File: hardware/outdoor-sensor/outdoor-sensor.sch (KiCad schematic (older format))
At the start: 11 parts, among them J1 POWER, J2 UART, SW1 RESET, SW2 BOOT, U1 ESP32-WROOM-32, U2 DS18B20

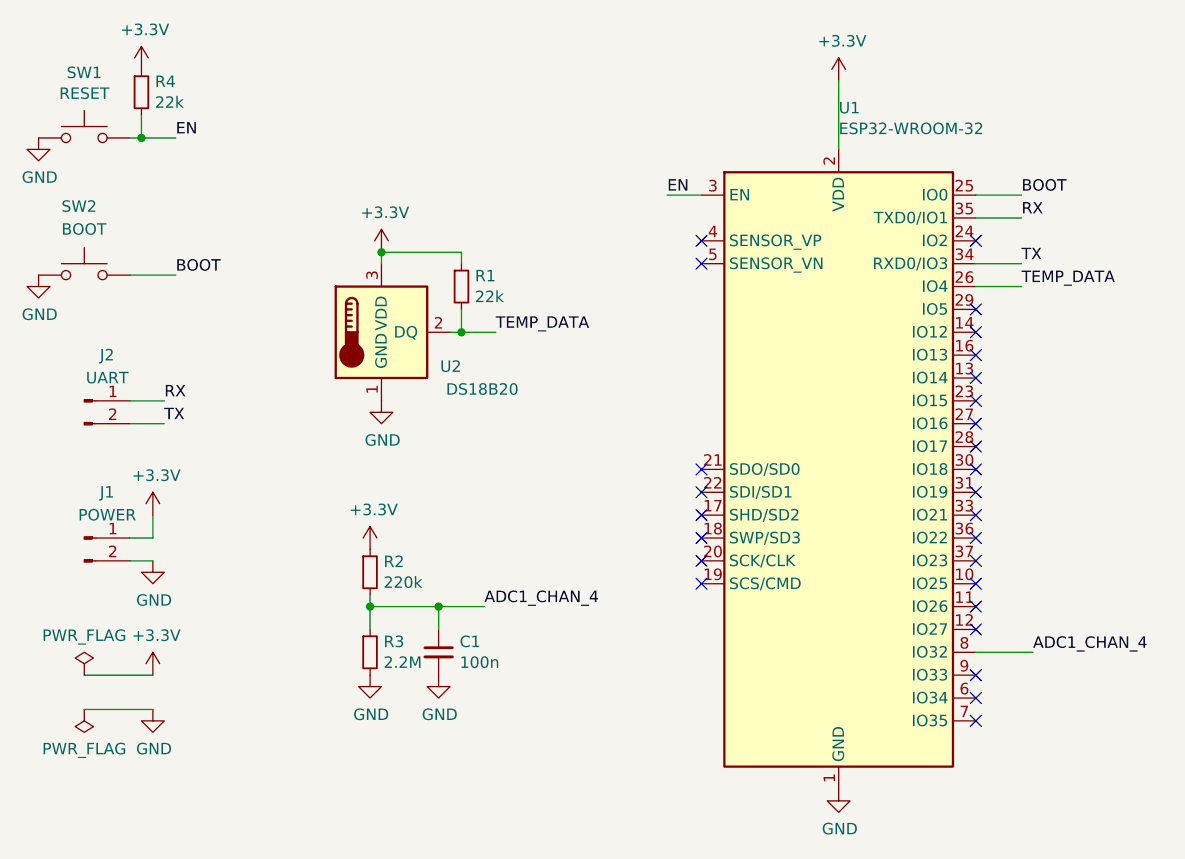
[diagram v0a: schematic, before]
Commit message: Swap out DS18B20 for DS18B20-PAR
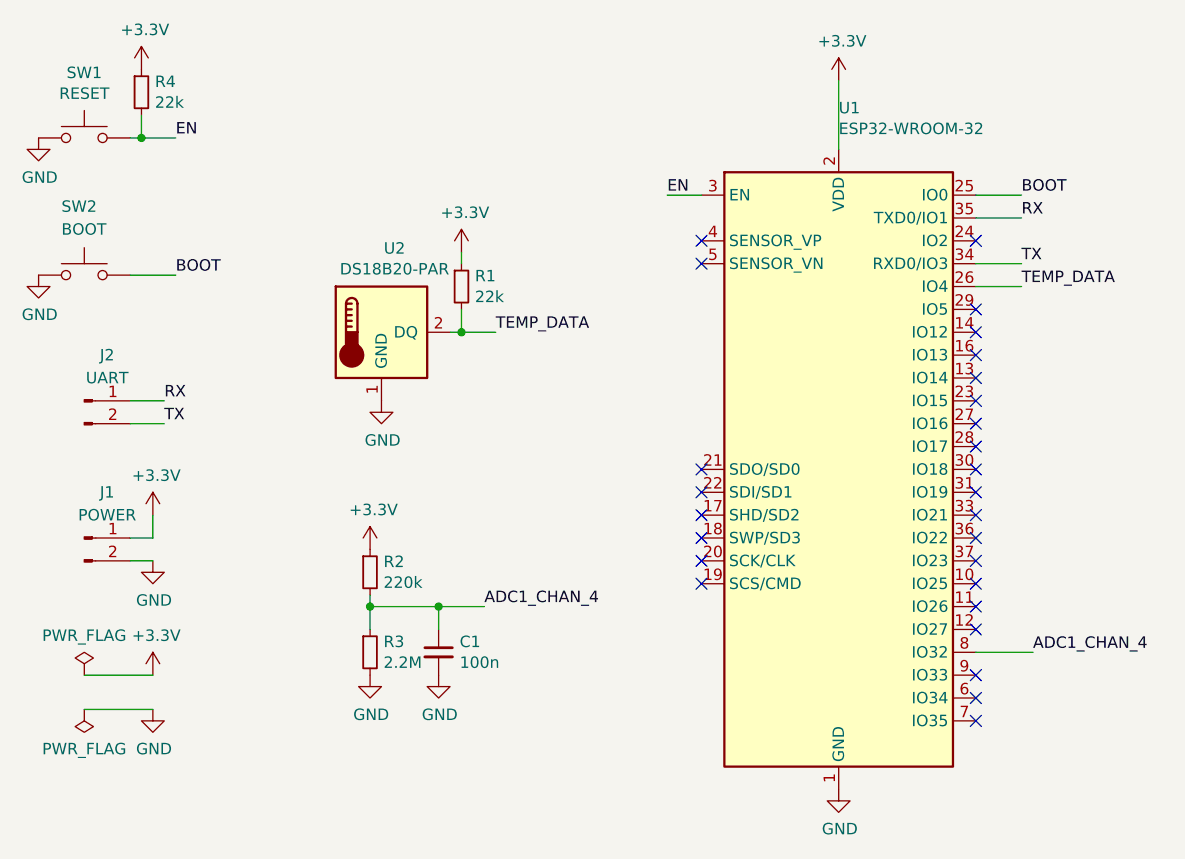
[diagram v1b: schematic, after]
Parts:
- removed U2: DS18B20, Package_TO_SOT_THT:TO-92_Inline, symbol Sensor_Temperature:DS18B20
- added U2: DS18B20-PAR, Package_TO_SOT_THT:TO-92_Inline, symbol Sensor_Temperature:DS18B20-PAR
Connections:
- net GND: now also U2.1 (GND)
- net TEMP_DATA: now also U2.2 (DQ)
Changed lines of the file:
@@
-	1    0    0    -1
-$EndComp
-$Comp
-L Sensor_Temperature:DS18B20 U2
-U 1 1 61550BDD
-P 4250 3050
-F 0 "U2" H 4600 2900 50  0000 R CNN
-F 1 "DS18B20" H 4850 2800 50  0000 R CNN
-F 2 "Package_TO_SOT_THT:TO-92_Inline" H 3250 2800 50  0001 C CNN
-F 3 "http://datasheets.maximintegrated.com/en/ds/DS18B20.pdf" H 4100 3300 50  0001 C CNN
-	1    4250 3050
 	1    0    0    -1
 $EndComp
@@
 L power:+3.3V #PWR0108
 U 1 1 61552A13
-P 4250 2700
-F 0 "#PWR0108" H 4250 2550 50  0001 C CNN
-F 1 "+3.3V" H 4265 2873 50  0000 C CNN
-F 2 "" H 4250 2700 50  0001 C CNN
-F 3 "" H 4250 2700 50  0001 C CNN
-	1    4250 2700
+P 4600 2700
+F 0 "#PWR0108" H 4600 2550 50  0001 C CNN
+F 1 "+3.3V" H 4615 2873 50  0000 C CNN
+F 2 "" H 4600 2700 50  0001 C CNN
+F 3 "" H 4600 2700 50  0001 C CNN
+	1    4600 2700
 	1    0    0    -1
 $EndComp
@@
 	4600 2950 4600 3050
 Wire Wire Line
-	4250 2700 4600 2700
-Wire Wire Line
 	4600 2700 4600 2750
-Wire Wire Line
-	4250 2700 4250 2750
-Connection ~ 4250 2700
 Wire Wire Line
 	6250 1950 6250 2250
@@
 Wire Wire Line
 	3250 3850 3250 3950
+$Comp
+L Sensor_Temperature:DS18B20-PAR U2
+U 1 1 616C9587
+P 4250 3050
+F 0 "U2" H 4307 3417 50  0000 C CNN
+F 1 "DS18B20-PAR" H 4307 3326 50  0000 C CNN
+F 2 "Package_TO_SOT_THT:TO-92_Inline" H 3250 2800 50  0001 C CNN
+F 3 "http://datasheets.maximintegrated.com/en/ds/DS18B20-PAR.pdf" H 4100 3300 50  0001 C CNN
+	1    4250 3050
+	1    0    0    -1
+$EndComp
 $EndSCHEMATC
